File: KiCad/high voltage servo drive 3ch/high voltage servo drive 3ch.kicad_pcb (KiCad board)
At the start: 4 copper layers, 109 x 231.4 mm, 486 parts, among them J1 8P8C_LED_Shielded_x2, J3 Conn_ARM_SWD_TagConnect_TC2030, J4 MOTOR_A, J5 MOTOR_B, J6 MOTOR_C, J7 DC BUS, J8 STO, M1 Fan_4pin, Q1 BSS83P, U1 STM32G473QET6, U10 TPS54202DDC, U12 OPA4323IPWR, U13 OPA4323IPWR, U14 OPA4323IPWR, U15 PC-817S1-CTP1-F, U16 PC-817S1-CTP1-F, U17 IPM, U18 IPM, U19 PC-817S1-CTP1-F, U2 IPM, U20 LNK306D, U21 TLV75733PDBV, U3 THVD1452, U4 THVD1452, U5 CA_IS3741HW, U6 TLV75733PDBV, U7 CA_IS3741HW, U8 CA_IS3741HW, U9 74LVC1G126, X1 16Mhz

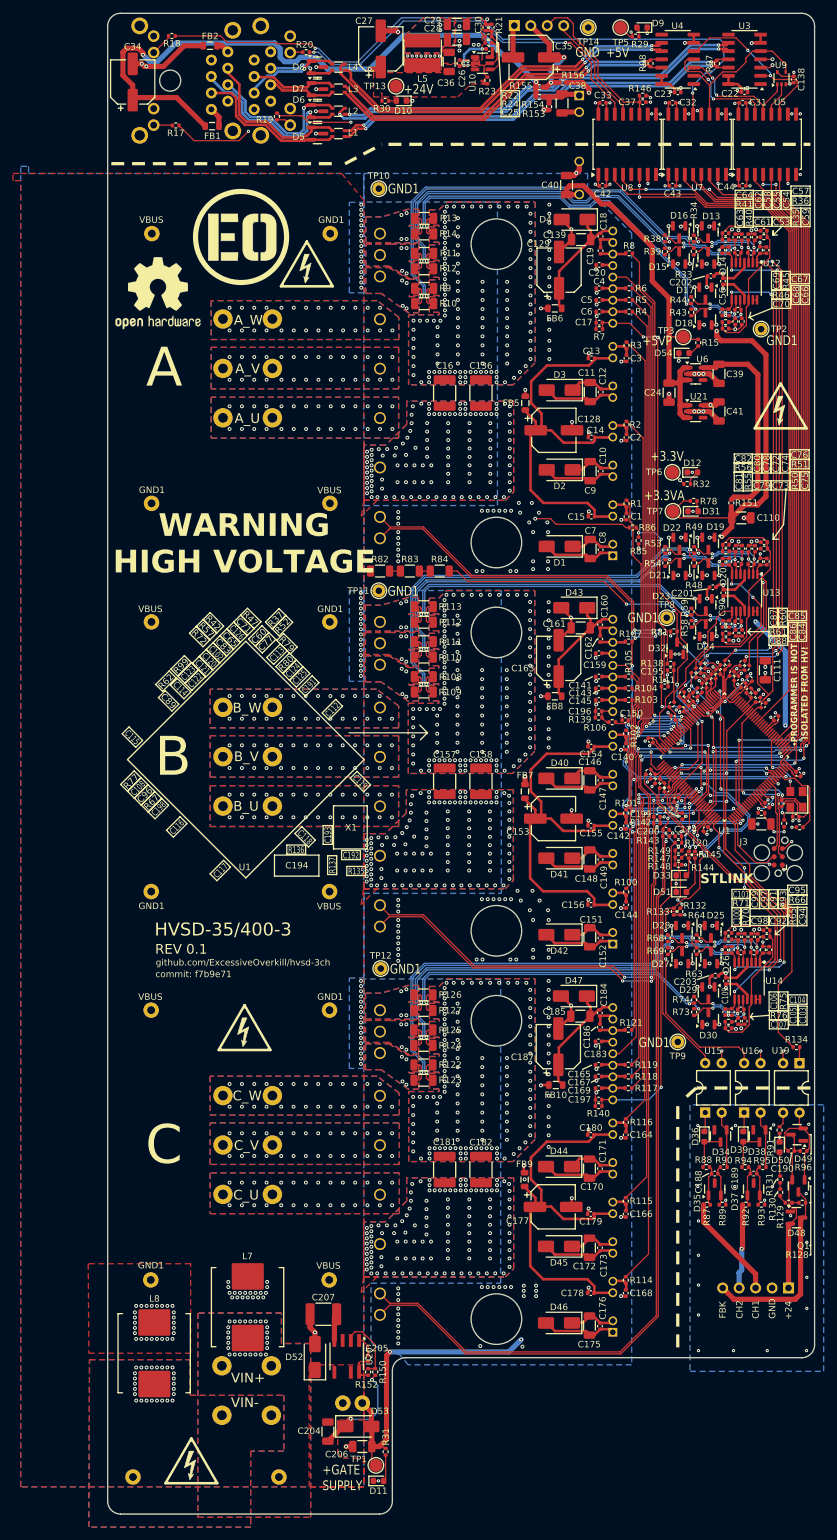
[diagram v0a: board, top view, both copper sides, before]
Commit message: add rev 0.2 changes and rev 0.1 mfg files
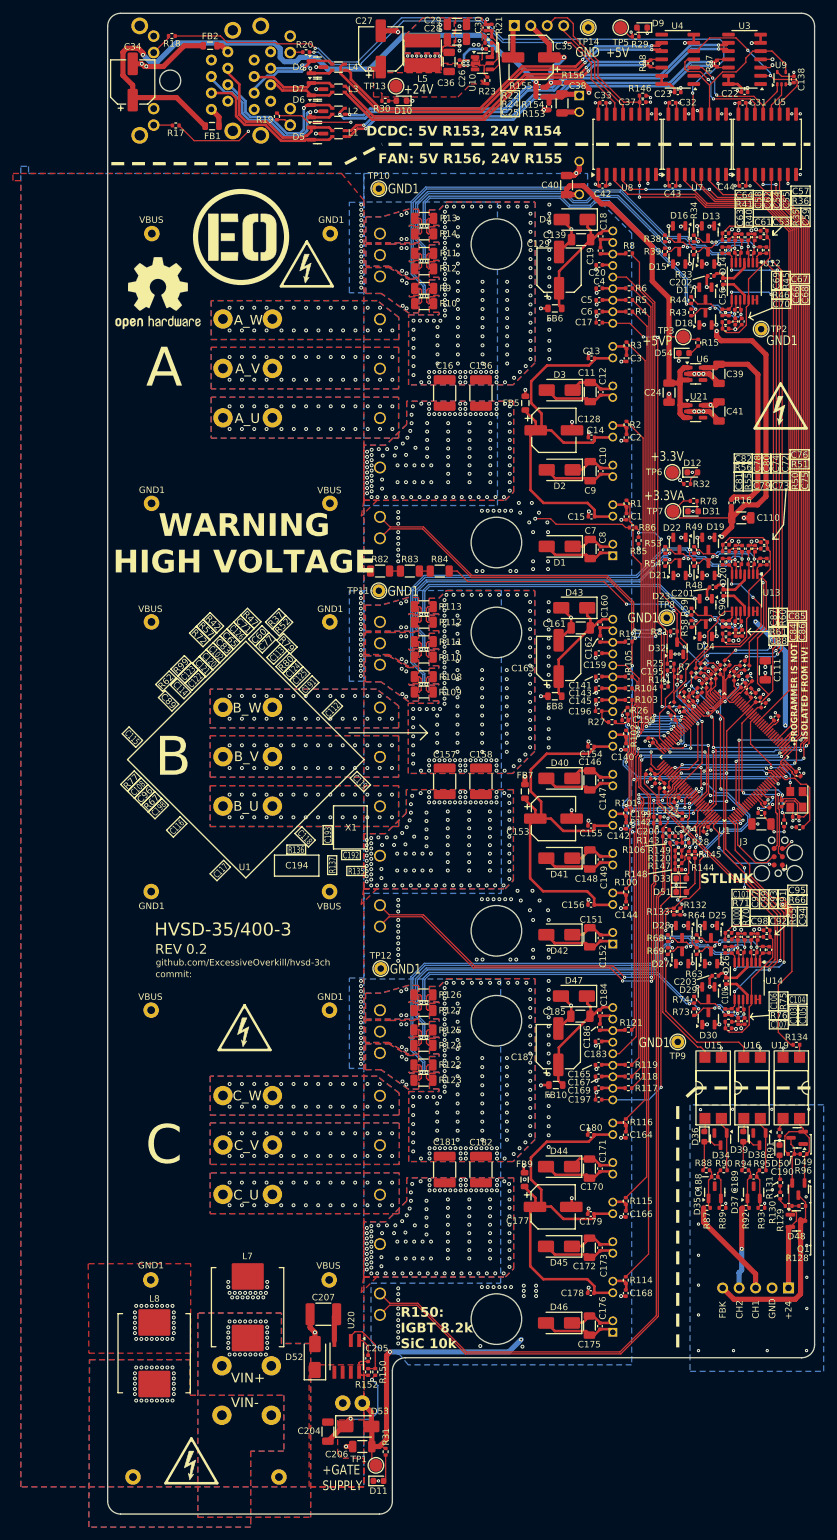
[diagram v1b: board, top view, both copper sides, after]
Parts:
- removed R138, R139, R140: 5.1k, Resistor_SMD:R_0402_1005Metric
- removed R151: 120, Resistor_SMD:R_0402_1005Metric
- added R16: 0, Resistor_SMD:R_0402_1005Metric, F.Cu at (252.4, 119.7)
- added R25: 12.1k, Resistor_SMD:R_0402_1005Metric, F.Cu at (243.1, 144.5)
- added R26: 12.1k, Resistor_SMD:R_0402_1005Metric, F.Cu at (236.4, 151.8)
- added R27: 12.1k, Resistor_SMD:R_0402_1005Metric, F.Cu at (234.0, 153.5)
- added R28: 12.1k, Resistor_SMD:R_0402_1005Metric, F.Cu at (245.3, 172.1)
- R106, R7: value 5.1k -> 12.1k
- R120: value 5.1k -> 100k
- R81: value 10k -> 12.1k
- U15, U16, U19: footprint Package_DIP:DIP-4_W7.62mm -> footprints:PC-817S1-CTP1-F
- U20: footprint Package_SO:PowerIntegrations_SO-8B -> Package_SO:PowerIntegrations_SO-8C
- U3, U4: value THVD1452 -> SP491EEN-L/TR
- X1: value 16Mhz -> 25Mhz
- moved R7 54.9 mm to (244.2, 146.5)
- moved R106 20.8 mm to (243.4, 172.1), turned to 180 degrees
- moved U19 4.01 mm to (261.6, 209.9)
- moved U15 3.99 mm to (249.6, 209.9)
- moved U16 3.99 mm to (255.6, 209.9)
- moved R120 2.14 mm to (244.2, 174.2), turned to 180 degrees
- moved C97 1.05 mm to (253.4, 186.6)
- moved C78 1.02 mm to (253.1, 126.8)
- moved C58 1.01 mm to (253.0, 78.7)
- moved C74 1.01 mm to (255.1, 126.8)
- moved C86 1.00 mm to (254.1, 139.8)
- moved C54 1.00 mm to (255.0, 78.7)
- moved C103 1.00 mm to (253.5, 199.6)
- moved C66 1.00 mm to (253.0, 91.7)
- moved C72 1.00 mm to (256.1, 126.8)
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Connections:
- R106 pad 1: Net-(U17-VTS) -> /INVERTER_C_TEMP
- R106 pad 2: /INVERTER_B_TEMP -> Net-(U18-VTS)
- R120 pad 1: Net-(U18-VTS) -> /Microcontroller/INVERTER_DISABLE
- R120 pad 2: /INVERTER_C_TEMP -> /INVERTER_DISABLE
- R7 pad 1: GND1 -> /INVERTER_A_TEMP
- R7 pad 2: Net-(U2-VTS) -> GND1
- R81 pad 1: /Microcontroller/VBUS_SENSE -> GND1
- R81 pad 2: GND1 -> /Microcontroller/VBUS_SENSE
- U1 pad 19: unconnected-(U1F-PF0-OSC_IN-Pad19) -> Net-(U1F-PF0-OSC_IN)
- U1 pad 8: Net-(U1C-PC14-OSC32_IN) -> unconnected-(U1C-PC14-OSC32_IN-Pad8)
- U12 pad 10: Net-(D18-common) -> Net-(D17-common)
- U12 pad 2: Net-(D13-common) -> Net-(D14-common)
- U12 pad 3: Net-(D14-common) -> Net-(D13-common)
- U12 pad 5: Net-(D16-common) -> Net-(D15-common)
- U12 pad 6: Net-(D15-common) -> Net-(D16-common)
- U12 pad 9: Net-(D17-common) -> Net-(D18-common)
- U13 pad 10: Net-(D24-common) -> Net-(D23-common)
- U13 pad 2: Net-(D19-common) -> Net-(D20-common)
- U13 pad 3: Net-(D20-common) -> Net-(D19-common)
- U13 pad 5: Net-(D22-common) -> Net-(D21-common)
- U13 pad 6: Net-(D21-common) -> Net-(D22-common)
- U13 pad 9: Net-(D23-common) -> Net-(D24-common)
- U14 pad 10: Net-(D30-common) -> Net-(D29-common)
- U14 pad 2: Net-(D25-common) -> Net-(D26-common)
- U14 pad 3: Net-(D26-common) -> Net-(D25-common)
- U14 pad 5: Net-(D28-common) -> Net-(D27-common)
- U14 pad 6: Net-(D27-common) -> Net-(D28-common)
- U14 pad 9: Net-(D29-common) -> Net-(D30-common)
- X1 pad 3: Net-(U1C-PC14-OSC32_IN) -> Net-(U1F-PF0-OSC_IN)
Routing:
- net Net-(U1F-PF0-OSC_IN): track 0.00 -> 15.4 mm, vias 0 -> 2
- net Net-(U1C-PC14-OSC32_IN): track 10.5 -> 0.00 mm, vias 2 -> 0
- net Net-(D22-common): track 20.9 -> 17.6 mm, vias 3 -> 2
- net Net-(D21-common): track 16.4 -> 19.4 mm
- net Net-(D15-common): track 16.6 -> 19.6 mm
- net Net-(D16-common): track 20.9 -> 17.9 mm, vias 3 -> 2
- net Net-(D28-common): track 20.9 -> 18.0 mm, vias 3 -> 2
- net Net-(D27-common): track 16.6 -> 19.4 mm
- net Net-(D23-common): track 11.6 -> 13.9 mm
- net Net-(D17-common): track 11.9 -> 14.1 mm
- net Net-(D29-common): track 11.9 -> 13.9 mm
- net GND1: track 278.9 -> 277.0 mm, vias 741 -> 743
- net Net-(D14-common): track 17.8 -> 16.1 mm, vias 3 -> 2
- net Net-(D20-common): track 17.8 -> 16.2 mm, vias 3 -> 2
- net Net-(D26-common): track 17.8 -> 16.3 mm, vias 3 -> 2
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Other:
- board text added: "DCDC: 5V R153, 24V R154"
- board text added: "FAN: 5V R156, 24V R155"
- board text added: "R150: IGBT 8.2k SiC 10k"
- board text added: "REV 0.2"
- board text added: "commit:"
- board text removed: "REV 0.1"
- board text removed: "commit: f7b9e71"
